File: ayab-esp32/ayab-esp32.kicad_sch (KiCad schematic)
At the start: 13 parts

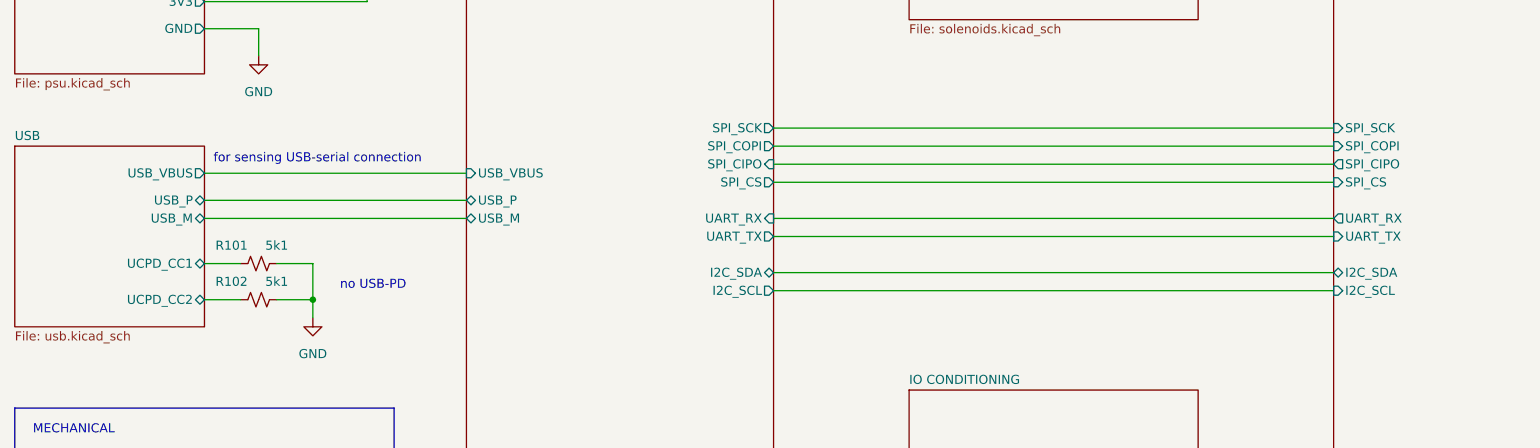
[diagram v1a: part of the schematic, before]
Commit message: fix comparator bias and hysteresis
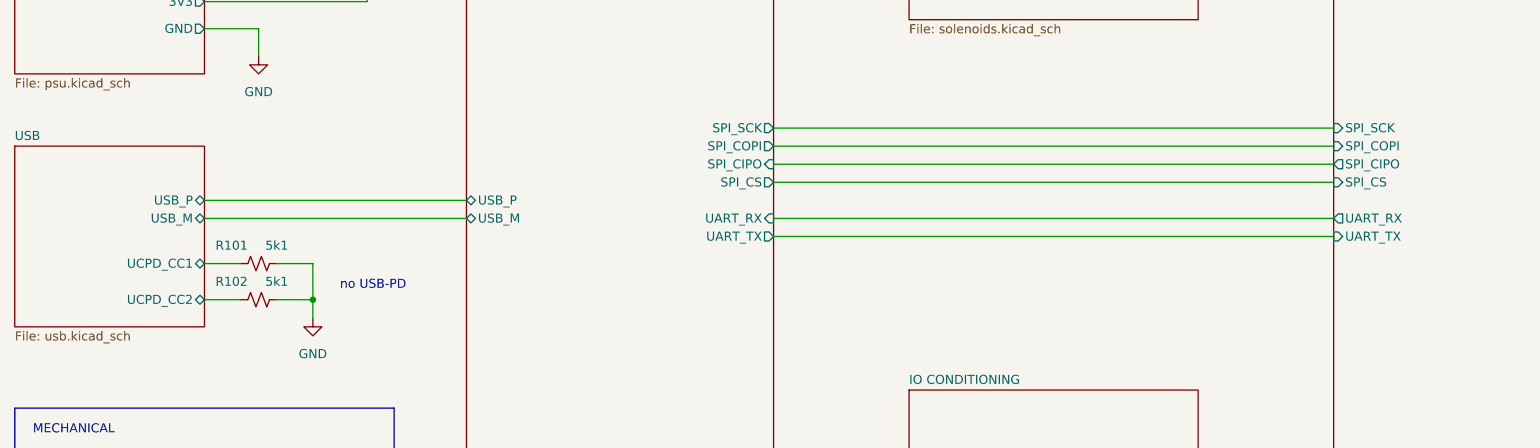
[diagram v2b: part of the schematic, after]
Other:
- sheet CONNECTORS ports: added none; removed I2C_SCL, I2C_SDA
- sheet ESP32 ports: added none; removed I2C_SCL, I2C_SDA, USB_VBUS
- sheet USB ports: added none; removed USB_VBUS
- note removed: "for sensing USB-serial connection"
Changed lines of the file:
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@@
     (comment 2 "distributed under CC-BY-SA-4.0")
   )
+  (bus_alias "MCU_SOL" (members "MCU_SOL_0" "MCU_SOL_1" "MCU_SOL_2" "MCU_SOL_4" "MCU_SOL_5" "MCU_SOL_6" "MCU_SOL_7" "MCU_SOL_8" "MCU_SOL_9" "MCU_SOL_A" "MCU_SOL_B" "MCU_SOL_C" "MCU_SOL_D" "MCU_SOL_E" "MCU_SOL_F" "MCU_SOL_3"))
   (bus_alias "SOL" (members "SOL_0" "SOL_1" "SOL_2" "SOL_3" "SOL_4" "SOL_5" "SOL_6" "SOL_7" "SOL_8" "SOL_9" "SOL_A" "SOL_B" "SOL_C" "SOL_D" "SOL_E" "SOL_F"))
-  (bus_alias "MCU_SOL" (members "MCU_SOL_0" "MCU_SOL_1" "MCU_SOL_2" "MCU_SOL_4" "MCU_SOL_5" "MCU_SOL_6" "MCU_SOL_7" "MCU_SOL_8" "MCU_SOL_9" "MCU_SOL_A" "MCU_SOL_B" "MCU_SOL_C" "MCU_SOL_D" "MCU_SOL_E" "MCU_SOL_F" "MCU_SOL_3"))
   (junction (at 81.28 139.7) (diameter 0) (color 0 0 0 0)
   )
@@
     (stroke (width 0) (type default))
   )
-  (wire (pts (xy 60.96 68.58) (xy 97.79 68.58))
-    (stroke (width 0) (type default))
-  )
   (wire (pts (xy 60.96 128.27) (xy 71.12 128.27))
     (stroke (width 0) (type default))
@@
     (stroke (width 0) (type default))
   )
-  (wire (pts (xy 140.97 85.09) (xy 219.71 85.09))
-    (stroke (width 0) (type default))
-  )
   (wire (pts (xy 40.64 128.27) (xy 50.8 128.27))
     (stroke (width 0) (type default))
@@
   )
   (wire (pts (xy 81.28 128.27) (xy 81.28 139.7))
-    (stroke (width 0) (type default))
-  )
-  (wire (pts (xy 140.97 82.55) (xy 219.71 82.55))
     (stroke (width 0) (type default))
   )
@@
     (effects (font (size 1.27 1.27)) (justify left bottom))
   )
-  (text "for sensing USB-serial connection" (at 62.23 67.31 0)
-    (effects (font (size 1.27 1.27)) (justify left bottom))
-  )
   (text "MECHANICAL" (at 36.83 105.41 0)
     (effects (font (size 1.27 1.27)) (justify left bottom))
@@
       (effects (font (size 1.27 1.27)) (justify right))
     )
-    (pin "USB_VBUS" output (at 60.96 68.58 0)
-      (effects (font (size 1.27 1.27)) (justify right))
-    )
     (instances
       (project "ayab-esp32"
@@
       (effects (font (size 1.27 1.27)) (justify left))
     )
-    (pin "I2C_SCL" input (at 219.71 85.09 180)
-      (effects (font (size 1.27 1.27)) (justify left))
-    )
     (pin "ENC_BELTPHASE" output (at 219.71 119.38 180)
       (effects (font (size 1.27 1.27)) (justify left))
     )
     (pin "ENC_V1" output (at 219.71 114.3 180)
-      (effects (font (size 1.27 1.27)) (justify left))
-    )
-    (pin "I2C_SDA" bidirectional (at 219.71 82.55 180)
       (effects (font (size 1.27 1.27)) (justify left))
     )
@@
       (effects (font (size 1.27 1.27)) (justify right))
     )
-    (pin "I2C_SDA" bidirectional (at 140.97 82.55 0)
-      (effects (font (size 1.27 1.27)) (justify right))
-    )
-    (pin "I2C_SCL" output (at 140.97 85.09 0)
-      (effects (font (size 1.27 1.27)) (justify right))
-    )
     (pin "USB_P" bidirectional (at 97.79 72.39 180)
       (effects (font (size 1.27 1.27)) (justify left))
@@
       (effects (font (size 1.27 1.27)) (justify right))
     )
-    (pin "USB_VBUS" input (at 97.79 68.58 180)
-      (effects (font (size 1.27 1.27)) (justify left))
-    )
     (pin "SPI_SCK" output (at 140.97 62.23 0)

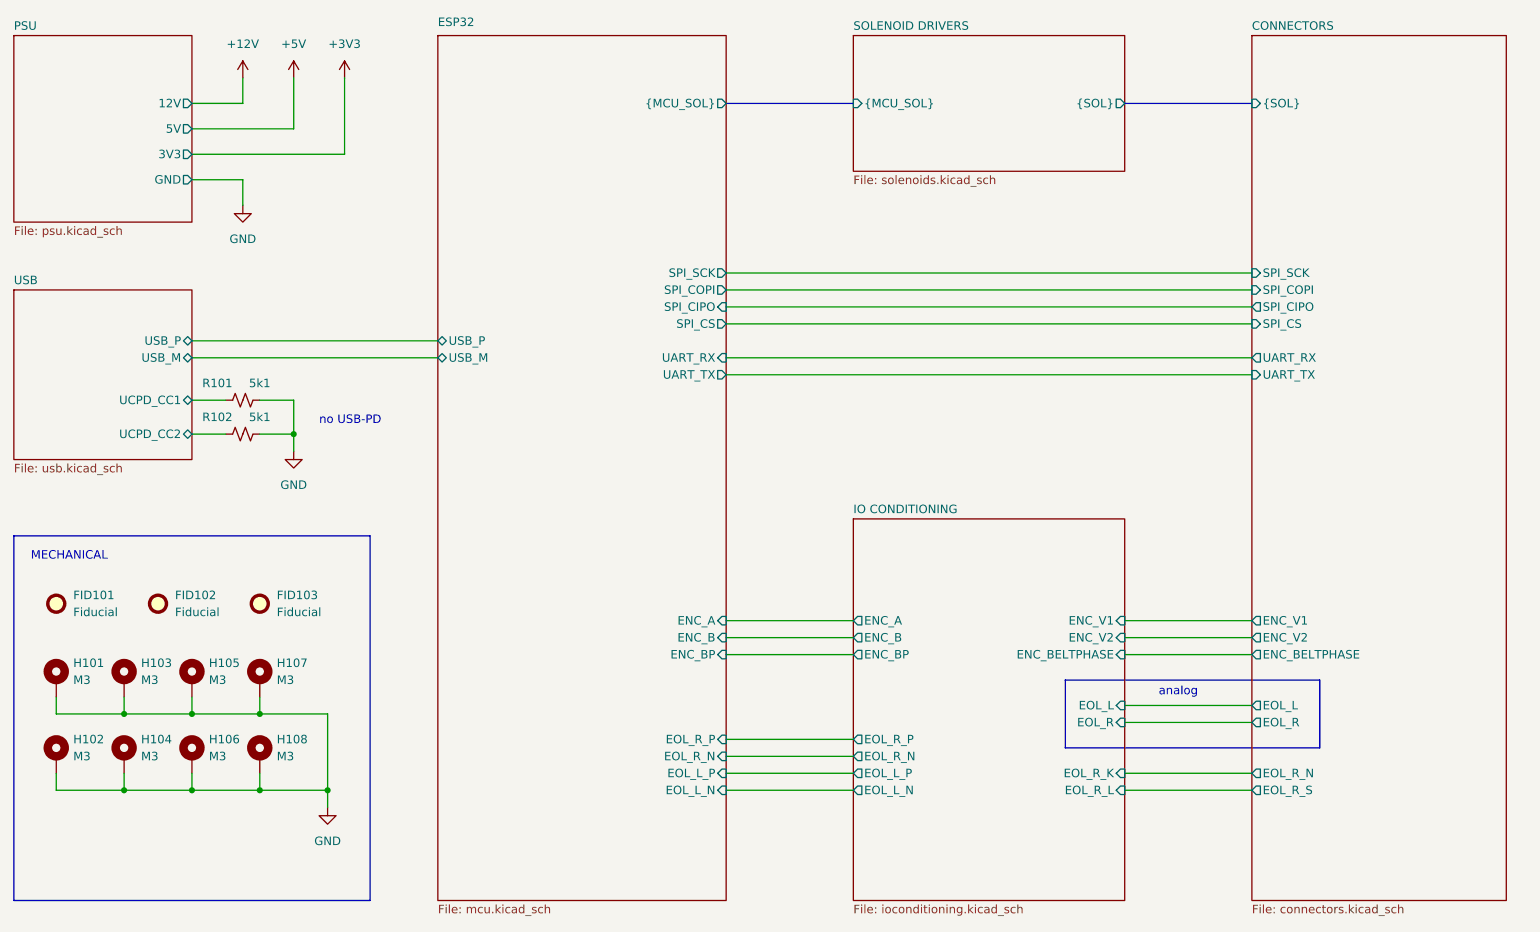
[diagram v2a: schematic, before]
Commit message: refactor for i2c expander
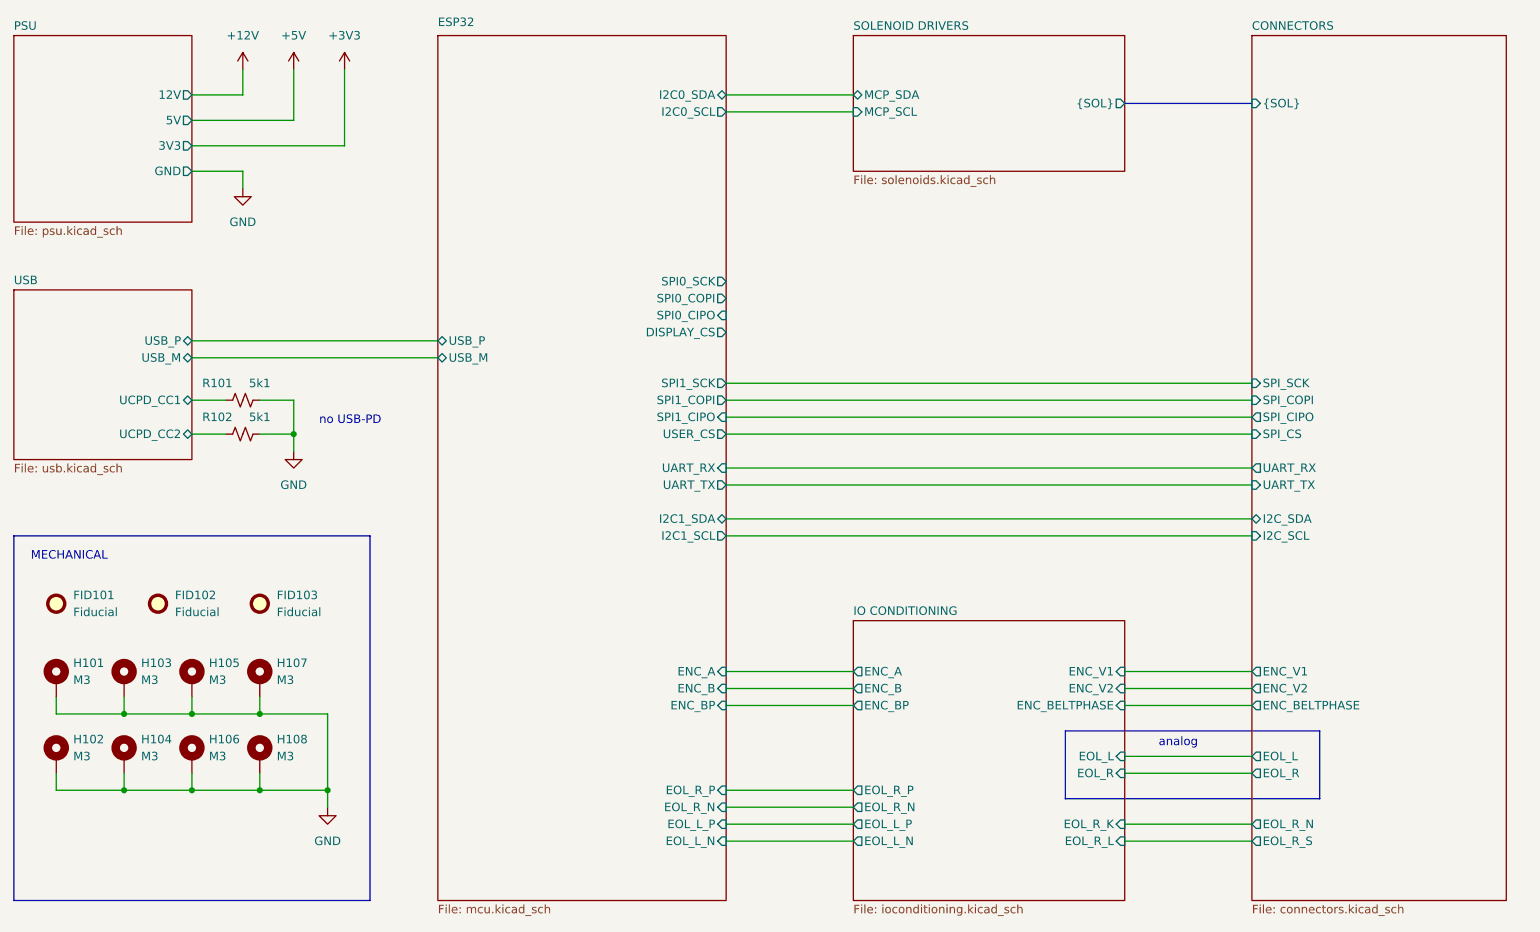
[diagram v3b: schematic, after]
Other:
- sheet CONNECTORS ports: added I2C_SCL, I2C_SDA; removed none
- sheet ESP32 ports: added DISPLAY_CS, I2C0_SCL, I2C0_SDA, I2C1_SCL, I2C1_SDA, SPI0_CIPO, SPI0_COPI, SPI0_SCK, SPI1_CIPO, SPI1_COPI, SPI1_SCK, USER_CS; removed SPI_CIPO, SPI_COPI, SPI_CS, SPI_SCK, {MCU_SOL}
- sheet SOLENOID DRIVERS ports: added MCP_SCL, MCP_SDA; removed {MCU_SOL}

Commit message: bidirectional level shifting
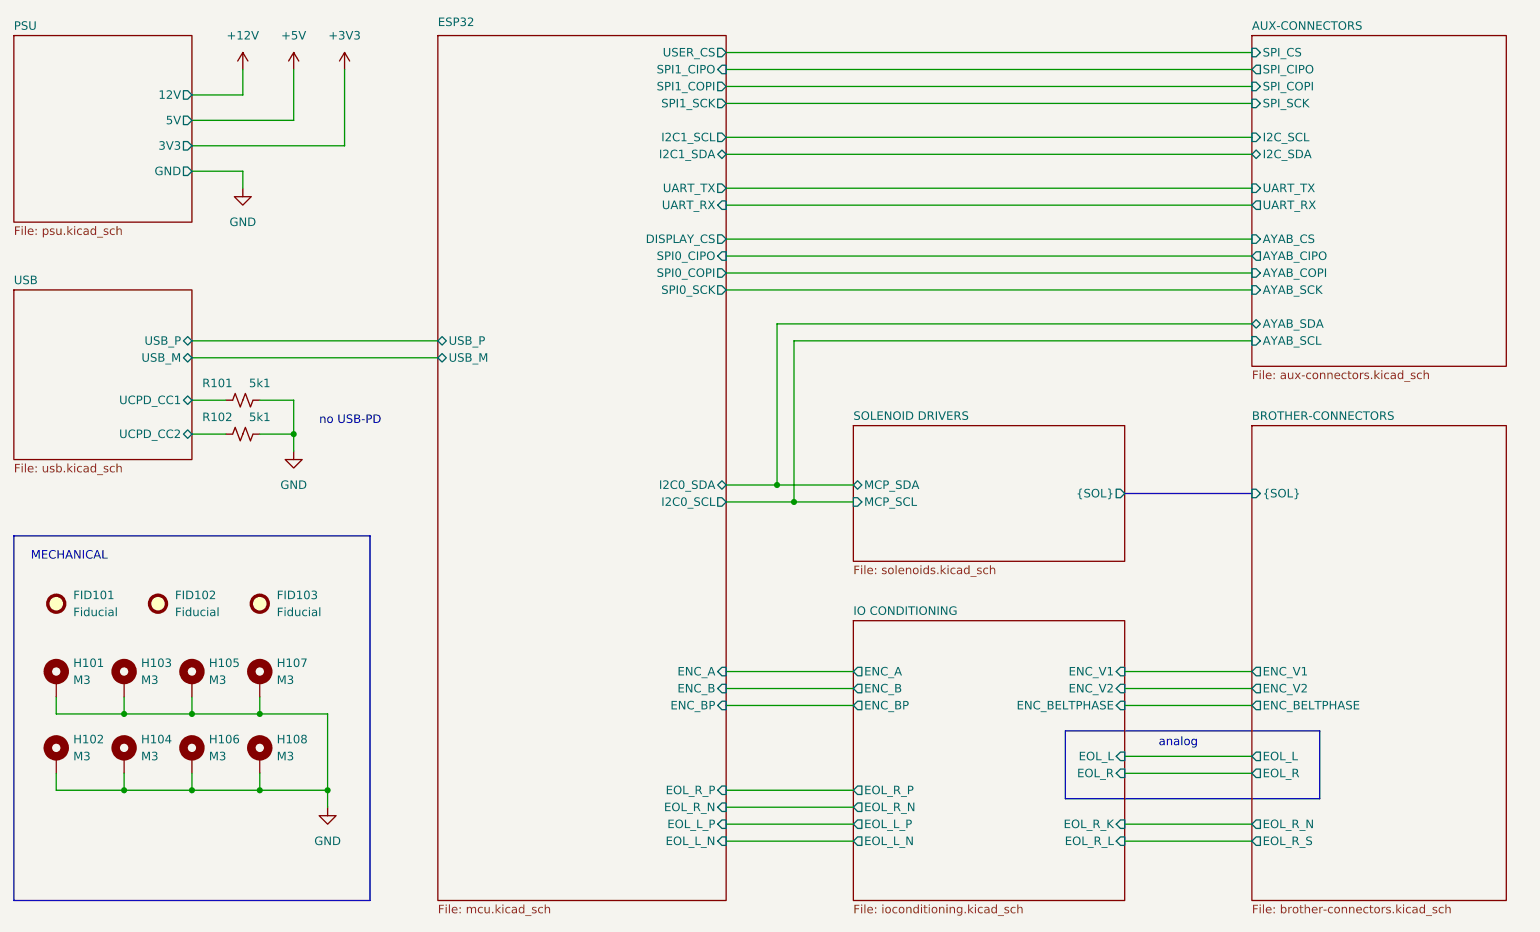
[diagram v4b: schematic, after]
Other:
- sheet CONNECTORS renamed BROTHER-CONNECTORS
- added sheet AUX-CONNECTORS (aux-connectors.kicad_sch)
- sheet BROTHER-CONNECTORS: file connectors.kicad_sch -> brother-connectors.kicad_sch
- sheet BROTHER-CONNECTORS ports: added none; removed I2C_SCL, I2C_SDA, SPI_CIPO, SPI_COPI, SPI_CS, SPI_SCK, UART_RX, UART_TX

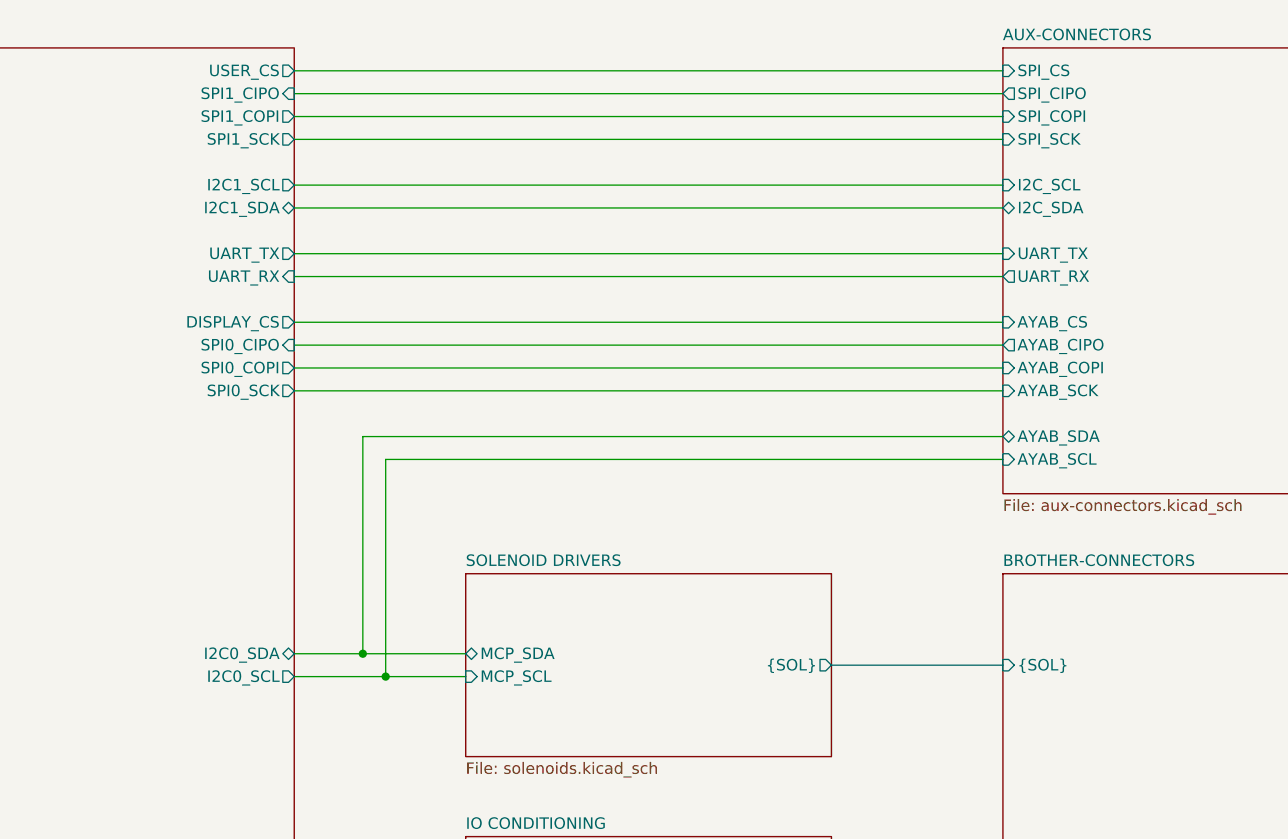
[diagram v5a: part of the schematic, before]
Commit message: add component selection, bom
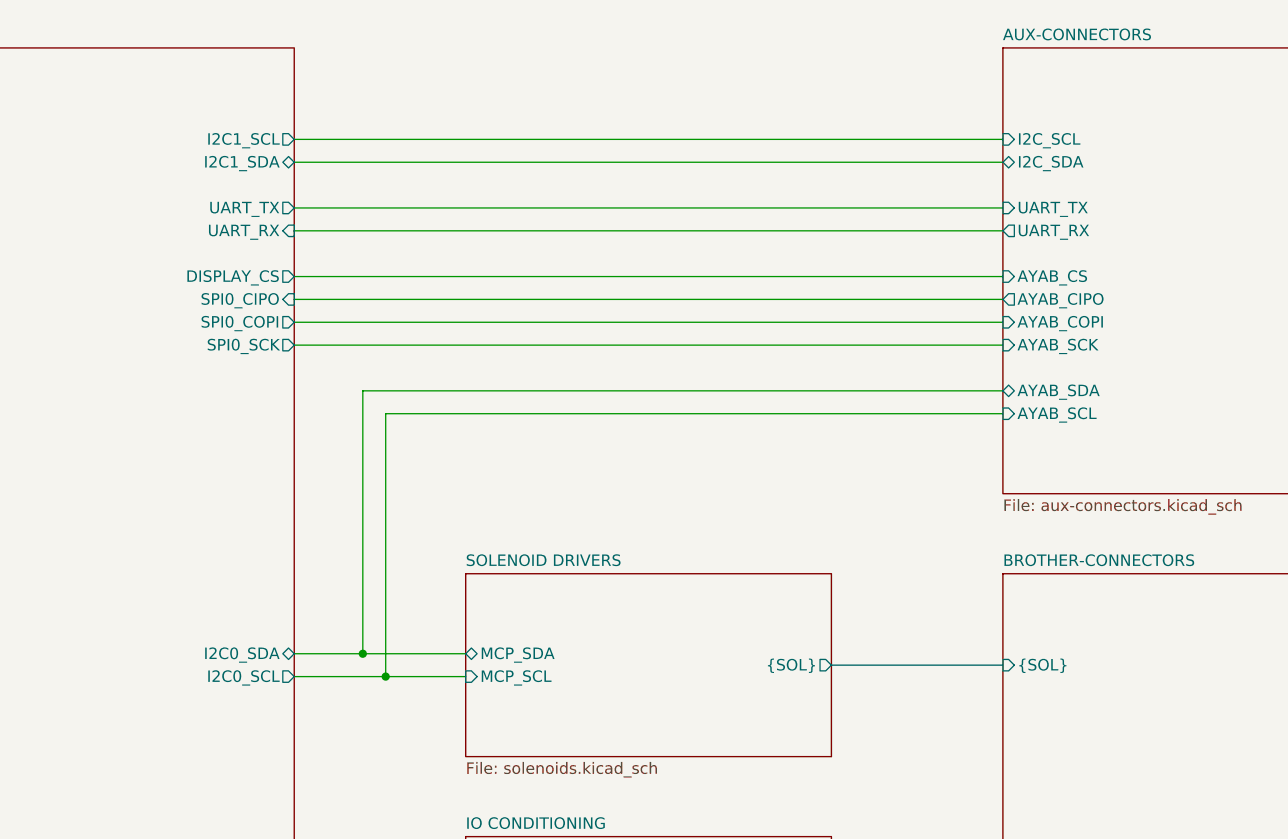
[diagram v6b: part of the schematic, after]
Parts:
- FID101, FID102, FID103: footprint (none) -> Fiducial:Fiducial_0.5mm_Mask1.5mm; symbol ayab-esp32:Fiducial -> Library:Fiducial; now left out of the parts list
- H101, H102, H103, H104, H105, H106, H107, H108: footprint (none) -> MountingHole:MountingHole_2.2mm_M2_DIN965_Pad; symbol ayab-esp32:MountingHole_Pad -> Library:MountingHole_Pad; now left out of the parts list
- R101, R102: footprint (none) -> Resistor_SMD:R_0603_1608Metric; symbol ayab-esp32:R_Small_US -> Library:R_Small_US; LCSC ID (none) -> C23186; OEM (none) -> UNI-ROYAL(Uniroyal Elec); OEM PN (none) -> 0603WAF5101T5E; Package (none) -> 0603
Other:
- sheet AUX-CONNECTORS ports: added none; removed SPI_CIPO, SPI_COPI, SPI_CS, SPI_SCK
- sheet ESP32 ports: added none; removed SPI1_CIPO, SPI1_COPI, SPI1_SCK, USER_CS
